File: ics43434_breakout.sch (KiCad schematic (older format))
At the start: 5 parts, among them J1 Conn_01x03_Male, J2 Conn_01x03_Male, U1 ICS-43434

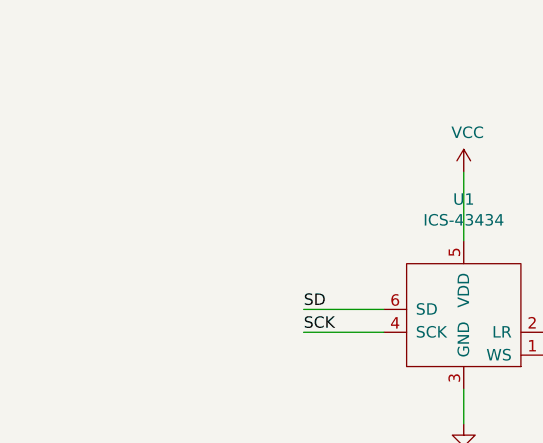
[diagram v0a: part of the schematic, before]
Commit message: add SD pull-down resistor
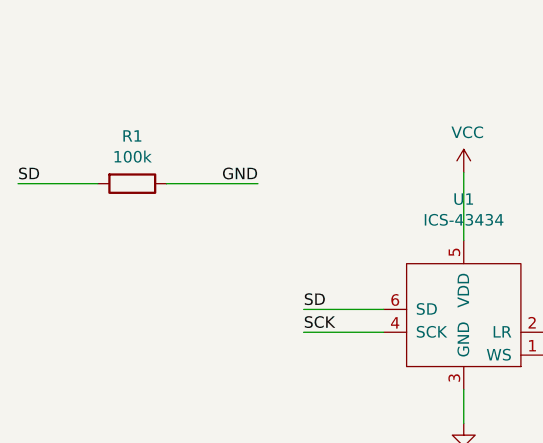
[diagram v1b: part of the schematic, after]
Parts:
- added R1: 100k, Resistor_SMD:R_0603_1608Metric_Pad1.05x0.95mm_HandSolder, symbol Device:R
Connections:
- wire segments 22 -> 24
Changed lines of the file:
@@
 	1    0    0    -1
 $EndComp
+$Comp
+L Device:R R1
+U 1 1 5E29CF02
+P 1550 1400
+F 0 "R1" V 1343 1400 50  0000 C CNN
+F 1 "100k" V 1434 1400 50  0000 C CNN
+F 2 "Resistor_SMD:R_0603_1608Metric_Pad1.05x0.95mm_HandSolder" V 1480 1400 50  0001 C CNN
+F 3 "~" H 1550 1400 50  0001 C CNN
+	1    1550 1400
+	0    1    1    0
+$EndComp
+Wire Wire Line
+	1400 1400 1050 1400
+Wire Wire Line
+	1700 1400 2100 1400
+Text Label 1050 1400 0    50   ~ 0
+SD
+Text Label 2100 1400 2    50   ~ 0
+GND
 $EndSCHEMATC

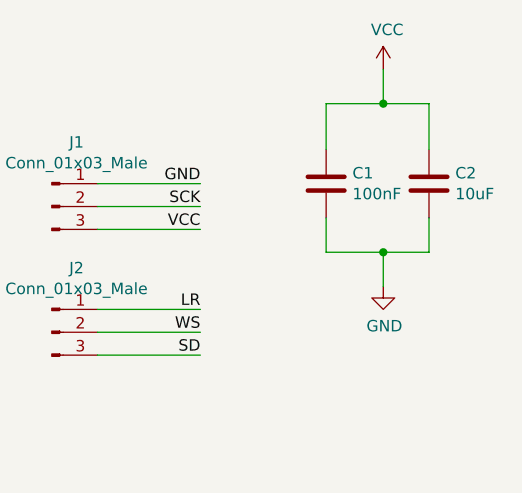
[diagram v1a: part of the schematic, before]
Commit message: remove 10uF capacitor
adapt layout
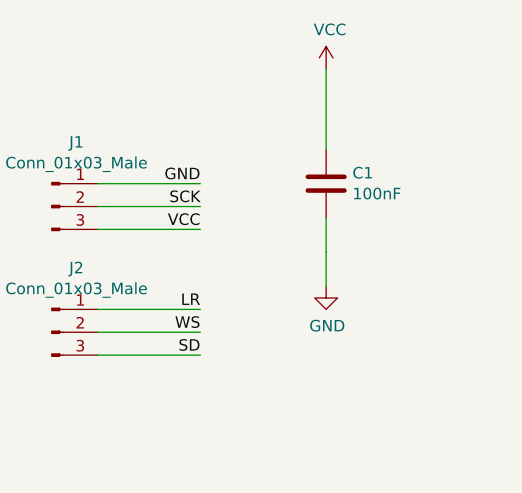
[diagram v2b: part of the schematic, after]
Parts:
- removed C2: 10uF, Capacitor_SMD:C_0603_1608Metric_Pad1.05x0.95mm_HandSolder, symbol Device:C
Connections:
- wire segments 24 -> 17
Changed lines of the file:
@@
-	1    0    0    -1
-$EndComp
-$Comp
-L Device:C C2
-U 1 1 5E296B74
-P 5700 1400
-F 0 "C2" H 5815 1446 50  0000 L CNN
-F 1 "10uF" H 5815 1355 50  0000 L CNN
-F 2 "Capacitor_SMD:C_0603_1608Metric_Pad1.05x0.95mm_HandSolder" H 5738 1250 50  0001 C CNN
-F 3 "~" H 5700 1400 50  0001 C CNN
-	1    5700 1400
 	1    0    0    -1
 $EndComp
 Wire Wire Line
-	5250 1250 5250 1050
-Wire Wire Line
-	5250 1050 5500 1050
-Wire Wire Line
-	5700 1050 5700 1250
-Wire Wire Line
-	5700 1550 5700 1700
-Wire Wire Line
-	5700 1700 5500 1700
-Wire Wire Line
 	5250 1700 5250 1550
 Wire Wire Line
-	5500 1700 5500 1850
-Connection ~ 5500 1700
-Wire Wire Line
-	5500 1700 5250 1700
-Wire Wire Line
-	5500 1050 5500 900
-Connection ~ 5500 1050
-Wire Wire Line
-	5500 1050 5700 1050
+	5250 1700 5250 1850
 $Comp
 L power:VCC #PWR0103
 U 1 1 5E298434
-P 5500 900
-F 0 "#PWR0103" H 5500 750 50  0001 C CNN
-F 1 "VCC" H 5517 1073 50  0000 C CNN
-F 2 "" H 5500 900 50  0001 C CNN
-F 3 "" H 5500 900 50  0001 C CNN
-	1    5500 900
+P 5250 900
+F 0 "#PWR0103" H 5250 750 50  0001 C CNN
+F 1 "VCC" H 5267 1073 50  0000 C CNN
+F 2 "" H 5250 900 50  0001 C CNN
+F 3 "" H 5250 900 50  0001 C CNN
+	1    5250 900
 	1    0    0    -1
 $EndComp
@@
 L power:GND #PWR0104
 U 1 1 5E298832
-P 5500 1850
-F 0 "#PWR0104" H 5500 1600 50  0001 C CNN
-F 1 "GND" H 5505 1677 50  0000 C CNN
-F 2 "" H 5500 1850 50  0001 C CNN
-F 3 "" H 5500 1850 50  0001 C CNN
-	1    5500 1850
+P 5250 1850
+F 0 "#PWR0104" H 5250 1600 50  0001 C CNN
+F 1 "GND" H 5255 1677 50  0000 C CNN
+F 2 "" H 5250 1850 50  0001 C CNN
+F 3 "" H 5250 1850 50  0001 C CNN
+	1    5250 1850
 	1    0    0    -1
 $EndComp
@@
 Text Label 2100 1400 2    50   ~ 0
 GND
+Wire Wire Line
+	5250 900  5250 1250
 $EndSCHEMATC
